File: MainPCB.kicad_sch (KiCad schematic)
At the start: 76 parts, among them IC1 VNH7070ASTR, IC2 VNH7070ASTR, IC3 VNH7070ASTR, IC4 VNH7070ASTR, IC5 VNH7070ASTR, J1 Conn_01x06, J10 Conn_01x02, J101 TYPEC-305-ACP16H458, J11 Conn_01x03, J20 Conn_01x02_Pin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

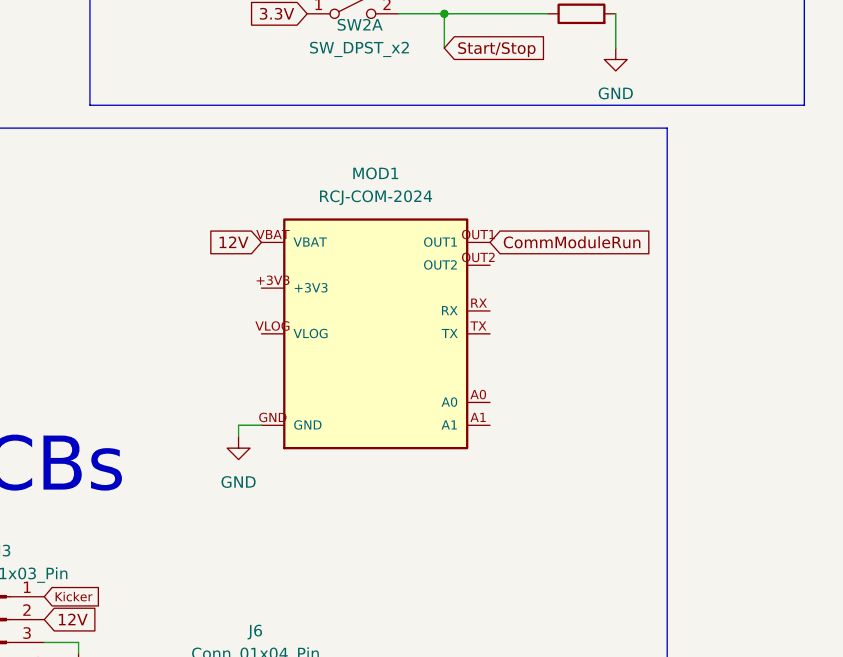
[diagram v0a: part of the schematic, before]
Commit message: Made changes to placement and HDMI is now vertical
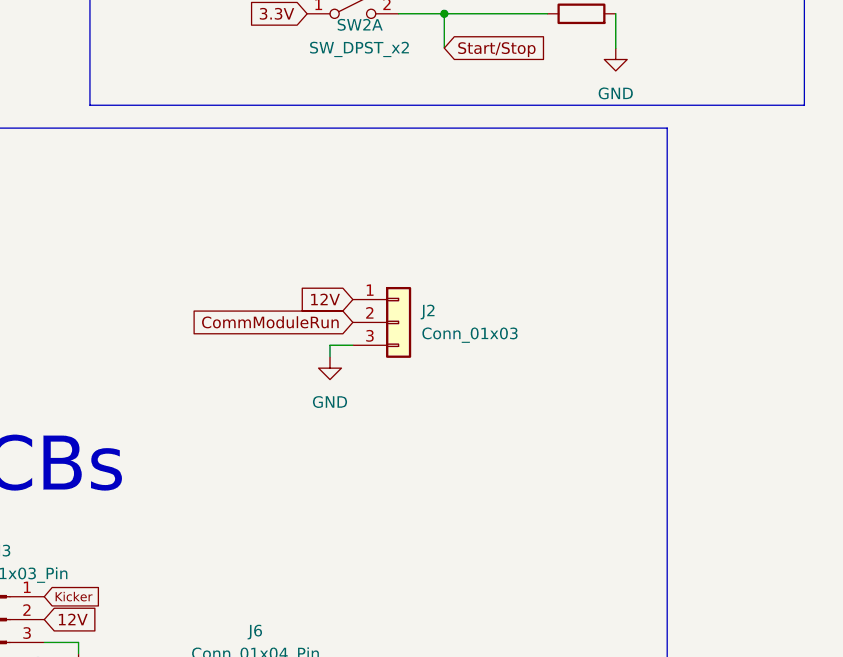
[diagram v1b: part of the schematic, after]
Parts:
- removed MOD1: RCJ-COM-2024, RCJ-COM-MOD:RCJ-COM-2024, symbol RCJ-COM-2024:RCJ-COM-2024
- added J2: Conn_01x03, Connector_JST:JST_XH_B3B-XH-A_1x03_P2.50mm_Vertical, symbol Connector_Generic:Conn_01x03
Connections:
- net 12V: now also J2.1 (Pin_1)
- net CommModuleRun: now also J2.2 (Pin_2)
- net GND: now also J2.3 (Pin_3)
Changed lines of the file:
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@@
 	(wire
 		(pts
-			(xy 119.38 191.77) (xy 119.38 193.04)
+			(xy 129.54 182.88) (xy 129.54 184.15)
 		)
 		(stroke
@@
 	(wire
 		(pts
-			(xy 121.92 191.77) (xy 119.38 191.77)
+			(xy 132.08 182.88) (xy 129.54 182.88)
 		)
 		(stroke
@@
 	(global_label "CommModuleRun"
 		(shape input)
-		(at 147.32 171.45 0)
+		(at 132.08 180.34 180)
 		(fields_autoplaced yes)
 		(effects
@@
 				(size 1.27 1.27)
 			)
-			(justify left)
+			(justify right)
 		)
 		(property "Intersheetrefs" "${INTERSHEET_REFS}"
-			(at 166.331 171.45 0)
+			(at 113.069 180.34 0)
 			(hide yes)
 			(show_name no)
@@
 					(size 1.27 1.27)
 				)
-				(justify left)
+				(justify right)
 			)
 		)
@@
 	(global_label "12V"
 		(shape input)
-		(at 121.92 171.45 180)
+		(at 132.08 177.8 180)
 		(fields_autoplaced yes)
 		(effects
@@
 		)
 		(property "Intersheetrefs" "${INTERSHEET_REFS}"
-			(at 115.4272 171.45 0)
+			(at 125.5872 177.8 0)
 			(hide yes)
 			(show_name no)
@@
 		(lib_name "GND_1")
 		(lib_id "power:GND")
-		(at 119.38 193.04 0)
+		(at 129.54 184.15 0)
 		(unit 1)
 		(body_style 1)
@@
 		(fields_autoplaced yes)
 		(property "Reference" "#PWR012"
-			(at 119.38 199.39 0)
+			(at 129.54 190.5 0)
 			(hide yes)
 			(show_name no)
@@
 		)
 		(property "Value" "GND"
-			(at 119.38 198.12 0)
+			(at 129.54 189.23 0)
 			(show_name no)
 			(do_not_autoplace no)
@@
 		)
 		(property "Footprint" ""
-			(at 119.38 193.04 0)
+			(at 129.54 184.15 0)
 			(hide yes)
 			(show_name no)
@@
 		)
 		(property "Datasheet" ""
-			(at 119.38 193.04 0)
+			(at 129.54 184.15 0)
 			(hide yes)
 			(show_name no)
@@
 		)
 		(property "Description" "Power symbol creates a global label with name \"GND\" , ground"
-			(at 119.38 193.04 0)
+			(at 129.54 184.15 0)
 			(hide yes)
 			(show_name no)
@@
 	)
 	(symbol
+		(lib_id "Connector_Generic:Conn_01x03")
+		(at 137.16 180.34 0)
+		(unit 1)
+		(body_style 1)
+		(exclude_from_sim no)
+		(in_bom yes)
+		(on_board yes)
+		(in_pos_files yes)
+		(dnp no)
+		(fields_autoplaced yes)
+		(property "Reference" "J2"
+			(at 139.7 179.0699 0)
+			(show_name no)
+			(do_not_autoplace no)
+			(effects
+				(font
+					(size 1.27 1.27)
+				)
+				(justify left)
+			)
+		)
+		(property "Value" "Conn_01x03"
+			(at 139.7 181.6099 0)
+			(show_name no)
+			(do_not_autoplace no)
+			(effects
+				(font
+					(size 1.27 1.27)
+				)
+				(justify left)
+			)
+		)
+		(property "Footprint" "Connector_JST:JST_XH_B3B-XH-A_1x03_P2.50mm_Vertical"
+			(at 137.16 180.34 0)
+			(hide yes)
+			(show_name no)
+			(do_not_autoplace no)
+			(effects
+				(font
+					(size 1.27 1.27)
+				)
+			)
+		)
+		(property "Datasheet" ""
+			(at 137.16 180.34 0)
+			(hide yes)
+			(show_name no)
+			(do_not_autoplace no)
+			(effects
+				(font
+					(size 1.27 1.27)
+				)
+			)
+		)
+		(property "Description" "Generic connector, single row, 01x03, script generated (kicad-library-utils/schlib/autogen/connector/)"
+			(at 137.16 180.34 0)
+			(hide yes)
+			(show_name no)
+			(do_not_autoplace no)
+			(effects
+				(font
+					(size 1.27 1.27)
+				)
+			)
+		)
+		(pin "2"
+		)
+		(pin "3"
+		)
+		(pin "1"
+		)
+		(instances
+			(project "MainPCB"
+				(path "/42b49b64-9684-402a-8d6b-7bff18ed389a"
+					(reference "J2")
+					(unit 1)
+				)
+			)
+		)
+	)
+	(symbol
 		(lib_name "MountingHole_1")
 		(lib_id "Mechanical:MountingHole")
@@
 					(unit 1)
 				)
-			)
-		)
-	)
-	(symbol
-		(lib_id "RCJ-COM-2024:RCJ-COM-2024")
-		(at 134.62 181.61 0)
-		(unit 1)
-		(body_style 1)
-		(exclude_from_sim no)
-		(in_bom yes)
-		(on_board yes)
-		(in_pos_files yes)
-		(dnp no)
-		(fields_autoplaced yes)
-		(property "Reference" "MOD1"
-			(at 134.62 163.83 0)
-			(show_name no)
-			(do_not_autoplace no)
-			(effects
-				(font
-					(size 1.27 1.27)
-				)
-			)
-		)
-		(property "Value" "RCJ-COM-2024"
-			(at 134.62 166.37 0)
-			(show_name no)
-			(do_not_autoplace no)
-			(effects
-				(font
-					(size 1.27 1.27)
-				)
-			)
-		)
-		(property "Footprint" "RCJ-COM-MOD:RCJ-COM-2024"
-			(at 134.62 181.61 0)
-			(hide yes)
-			(show_name no)
-			(do_not_autoplace no)
-			(effects
-				(font
-					(size 1.27 1.27)
-				)
-				(justify bottom)
-			)
-		)
-		(property "Datasheet" ""
-			(at 134.62 181.61 0)
-			(hide yes)
-			(show_name no)
-			(do_not_autoplace no)
-			(effects
-				(font
-					(size 1.27 1.27)
-				)
-			)
-		)
-		(property "Description" ""
-			(at 134.62 181.61 0)
-			(hide yes)
-			(show_name no)
-			(do_not_autoplace no)
-			(effects
-				(font
-					(size 1.27 1.27)
-				)
-			)
-		)
-		(pin "A0"
-		)
-		(pin "RX"
-		)
-		(pin "OUT2"
-		)
-		(pin "A1"
-		)
-		(pin "+3V3"
-		)
-		(pin "OUT1"
-		)
-		(pin "GND"
-		)
-		(pin "VLOG"
-		)
-		(pin "VBAT"
-		)
-		(pin "TX"
-		)
-		(instances
-			(project "MainPCB"
-				(path "/42b49b64-9684-402a-8d6b-7bff18ed389a"
-					(reference "MOD1")
-					(unit 1)
-				)

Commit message: Fixed Errors
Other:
- moved on the sheet: TP103
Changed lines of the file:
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@@
 	)
 	(junction
-		(at 648.97 59.69)
-		(diameter 0)
-		(color 0 0 0 0)
-	)
-	(junction
 		(at 297.18 55.88)
 		(diameter 0)
@@
 	(wire
 		(pts
+			(xy 626.11 46.99) (xy 626.11 49.53)
+		)
+		(stroke
+			(width 0)
+			(type default)
+		)
+	)
+	(wire
+		(pts
 			(xy 646.43 107.95) (xy 687.07 107.95)
 		)
@@
 	(wire
 		(pts
-			(xy 648.97 49.53) (xy 648.97 59.69)
-		)
-		(stroke
-			(width 0)
-			(type default)
-		)
-	)
-	(wire
-		(pts
 			(xy 63.5 312.42) (xy 66.04 312.42)
 		)
@@
 	(wire
 		(pts
-			(xy 648.97 59.69) (xy 648.97 67.31)
-		)
-		(stroke
-			(width 0)
-			(type default)
-		)
-	)
-	(wire
-		(pts
 			(xy 162.56 391.16) (xy 162.56 394.97)
 		)
@@
 	(wire
 		(pts
-			(xy 648.97 67.31) (xy 646.43 67.31)
-		)
-		(stroke
-			(width 0)
-			(type default)
-		)
-	)
-	(wire
-		(pts
 			(xy 162.56 355.6) (xy 162.56 360.68)
 		)
@@
 	(symbol
 		(lib_id "Connector:TestPoint_Small")
-		(at 648.97 59.69 0)
+		(at 626.11 49.53 0)
 		(mirror y)
 		(unit 1)
@@
 		(dnp no)
 		(property "Reference" "TP103"
-			(at 647.7 58.4199 0)
+			(at 624.84 48.2599 0)
 			(show_name no)
 			(do_not_autoplace no)
@@
 		)
 		(property "Value" "+3V3_PI"
-			(at 647.7 60.9599 0)
+			(at 624.84 50.7999 0)
 			(show_name no)
 			(do_not_autoplace no)
@@
 		)
 		(property "Footprint" "TestPoint:TestPoint_Pad_D1.0mm"
-			(at 643.89 59.69 0)
+			(at 621.03 49.53 0)
 			(hide yes)
 			(show_name no)
@@
 		)
 		(property "Datasheet" ""
-			(at 643.89 59.69 0)
+			(at 621.03 49.53 0)
 			(hide yes)
 			(show_name no)
@@
 		)
 		(property "Description" "test point"
-			(at 648.97 59.69 0)
+			(at 626.11 49.53 0)
 			(hide yes)
 			(show_name no)
@@
 	(symbol
 		(lib_id "power:+3V3")
-		(at 648.97 49.53 0)
+		(at 626.11 46.99 0)
 		(unit 1)
 		(body_style 1)
@@
 		(fields_autoplaced yes)
 		(property "Reference" "#PWR0111"
-			(at 648.97 53.34 0)
+			(at 626.11 50.8 0)
 			(hide yes)
 			(show_name no)
@@
 		)
 		(property "Value" "+3V3_PI"
-			(at 651.51 48.2599 0)
+			(at 628.65 45.7199 0)
 			(show_name no)
 			(do_not_autoplace no)
@@
 		)
 		(property "Footprint" ""
-			(at 648.97 49.53 0)
+			(at 626.11 46.99 0)
 			(hide yes)
 			(show_name no)
@@
 		)
 		(property "Datasheet" ""
-			(at 648.97 49.53 0)
+			(at 626.11 46.99 0)
 			(hide yes)
 			(show_name no)
@@
 		)
 		(property "Description" "Power symbol creates a global label with name \"+3V3\""
-			(at 648.97 49.53 0)
+			(at 626.11 46.99 0)
 			(hide yes)
 			(show_name no)
